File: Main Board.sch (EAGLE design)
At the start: 25 parts, among them IC1 TB6612FNG, U1 TPS61030RSAR

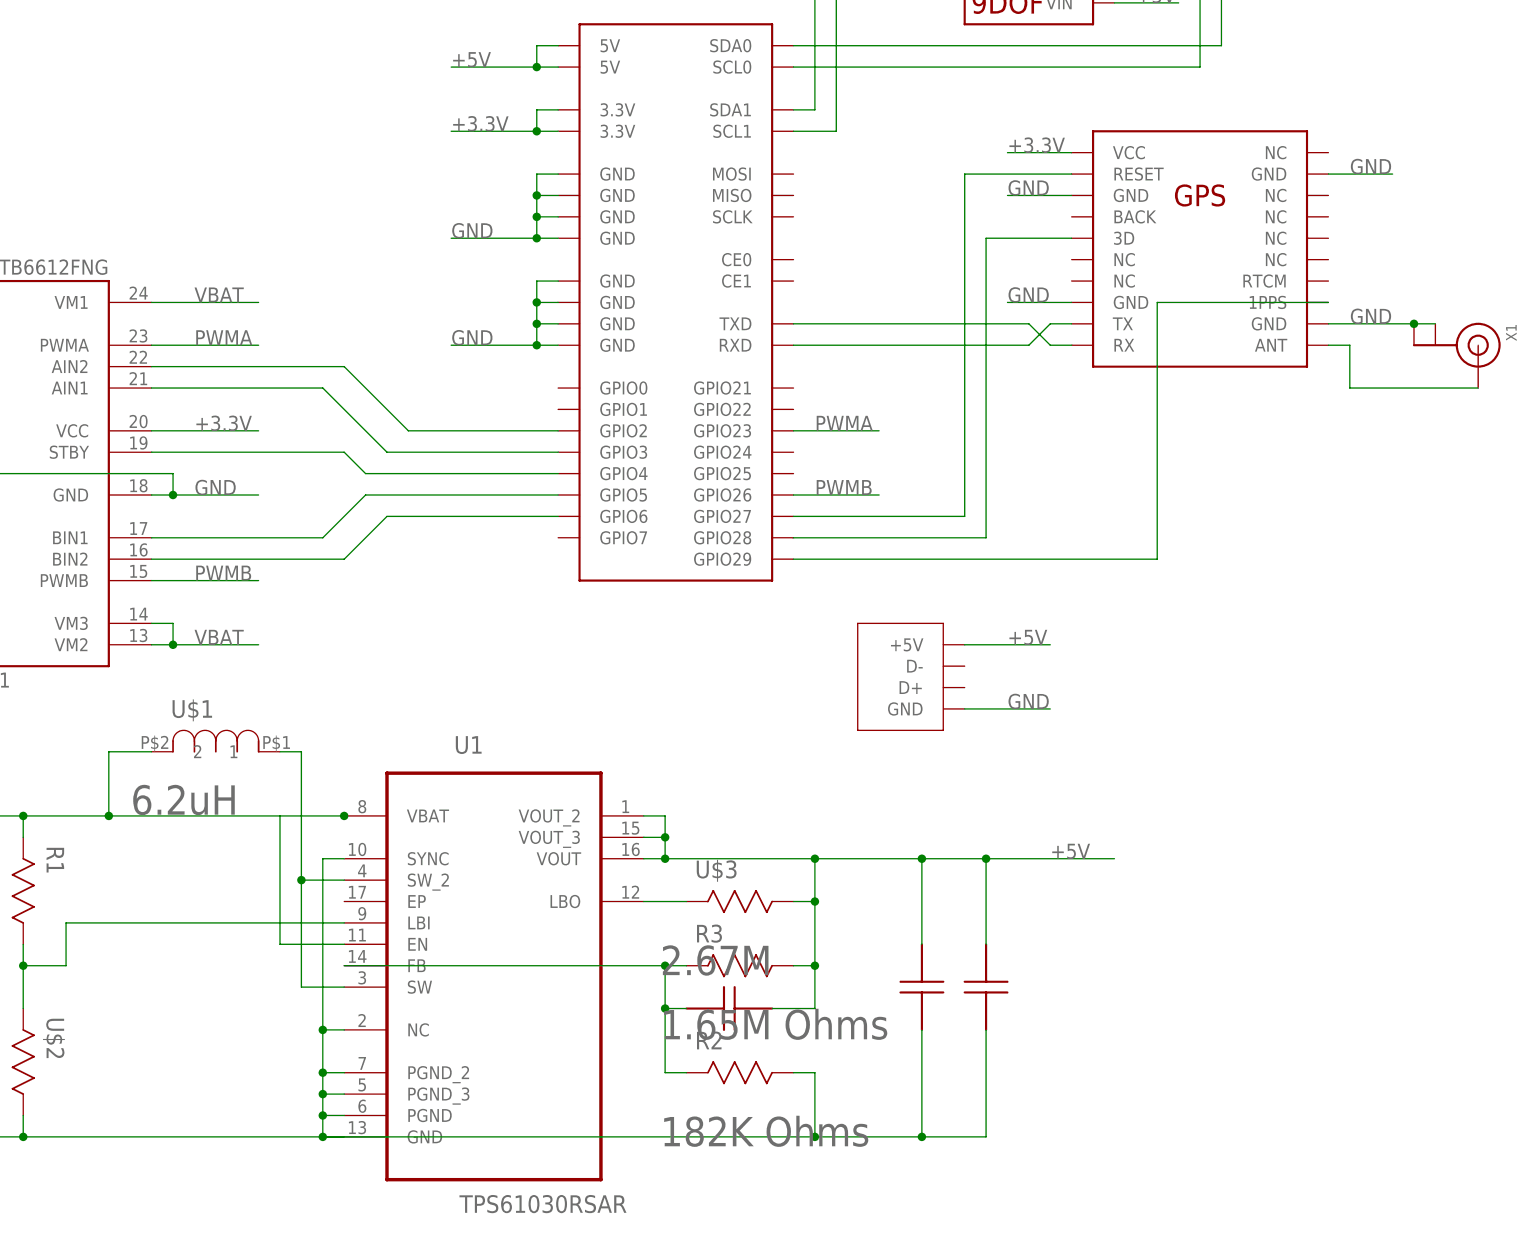
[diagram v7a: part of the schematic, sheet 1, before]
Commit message: Added Ground Pours
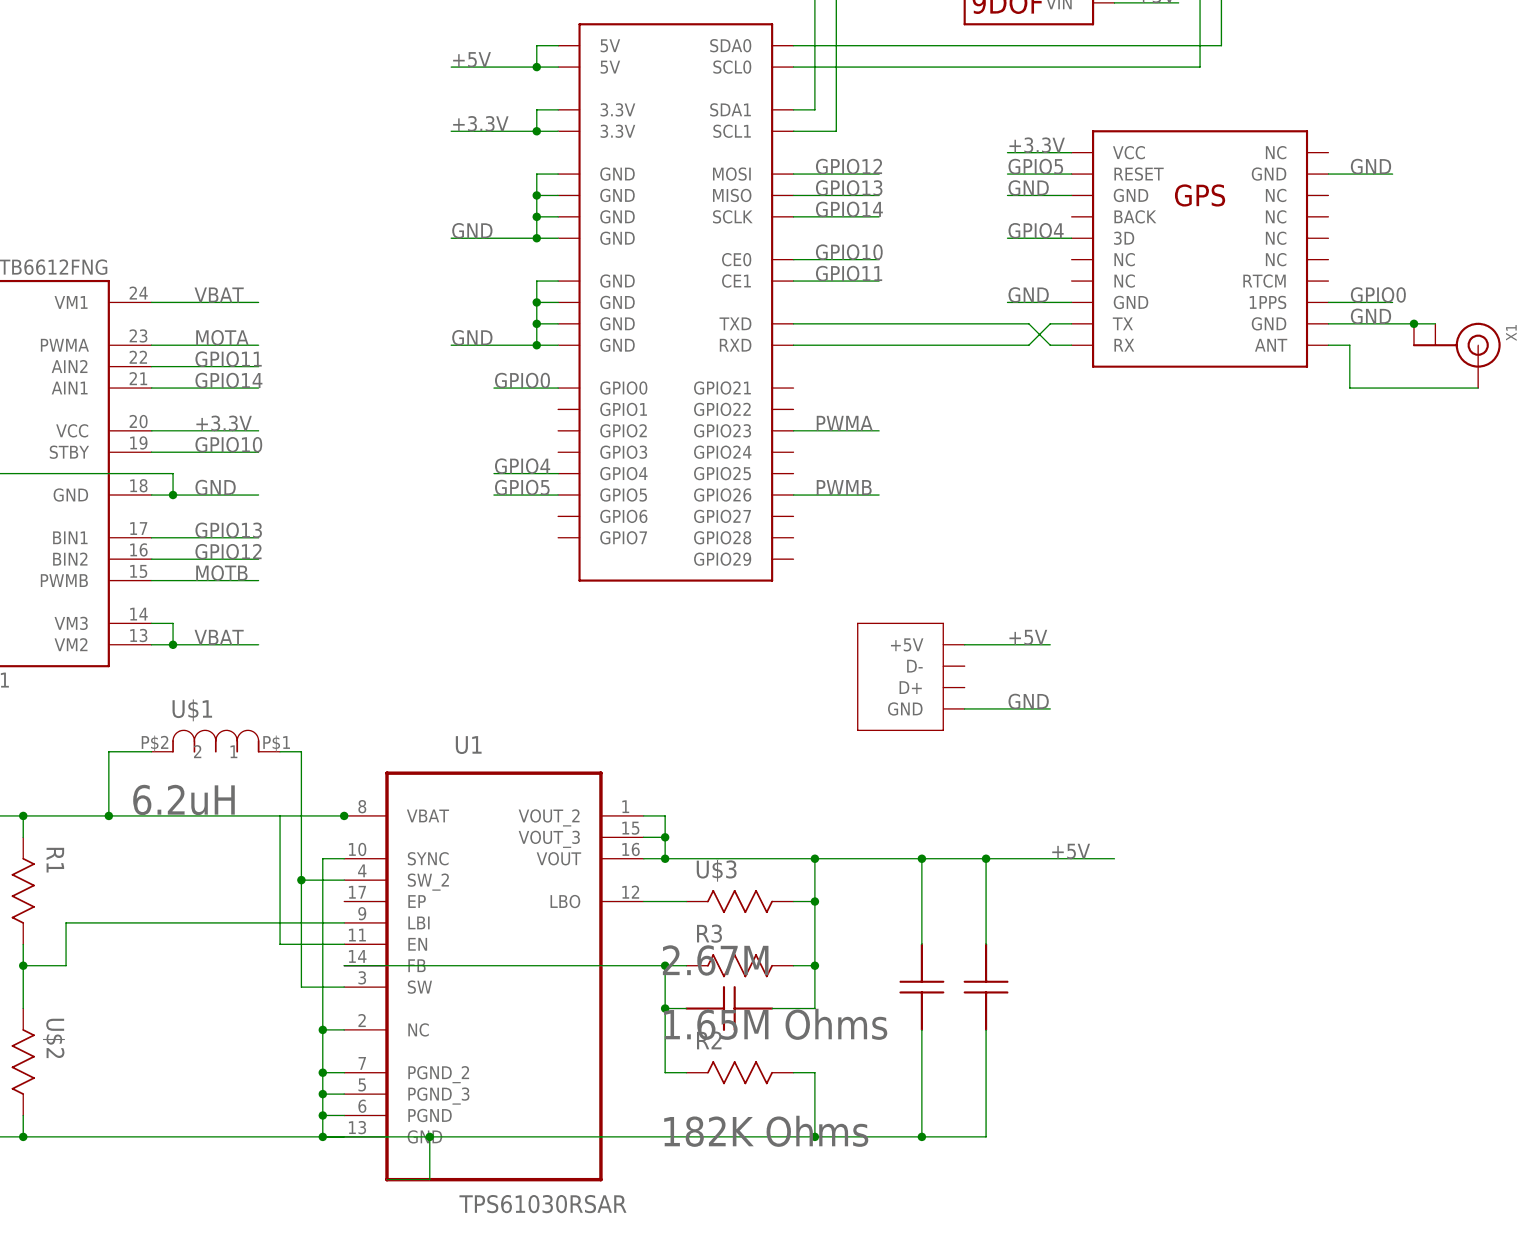
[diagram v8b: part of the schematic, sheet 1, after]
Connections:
- removed net N$15: IC1.AIN2, U$11.GPIO2
- removed net N$20: IC1.AIN1, U$11.GPIO3
- removed net N$21: IC1.STBY, U$11.GPIO4
- removed net N$22: IC1.BIN1, U$11.GPIO5
- removed net N$23: IC1.BIN2, U$11.GPIO6
- removed net N$5: U$11.GPIO27, U$5.RESET
- removed net N$6: U$11.GPIO28, U$5.3D
- removed net N$9: U$11.GPIO29, U$5.1PPS
- new net GPIO0: U$11.GPIO0, U$5.1PPS
- new net GPIO10: IC1.STBY, U$11.CE0
- new net GPIO11: IC1.AIN2, U$11.CE1
- new net GPIO12: IC1.BIN2, U$11.MOSI
- new net GPIO13: IC1.BIN1, U$11.MISO
- new net GPIO14: IC1.AIN1, U$11.SCLK
- new net GPIO4: U$11.GPIO4, U$5.3D
- new net GPIO5: U$11.GPIO5, U$5.RESET
- new net MOTA: IC1.PWMA
- new net MOTB: IC1.PWMB
- net PWMA: no longer IC1.PWMA
- net PWMB: no longer IC1.PWMB
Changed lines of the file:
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@@
 <wire x1="60.96" y1="-22.86" x2="53.34" y2="-22.86" width="0.1524" layer="91"/>
 <wire x1="53.34" y1="-22.86" x2="33.02" y2="-22.86" width="0.1524" layer="91"/>
-<wire x1="111.76" y1="-22.86" x2="170.18" y2="-22.86" width="0.1524" layer="91"/>
+<wire x1="111.76" y1="-22.86" x2="124.46" y2="-22.86" width="0.1524" layer="91"/>
 <label x="43.18" y="-22.86" size="1.778" layer="95"/>
 <pinref part="U$7" gate="G$1" pin="P$2"/>
+<wire x1="124.46" y1="-22.86" x2="170.18" y2="-22.86" width="0.1524" layer="91"/>
 <wire x1="170.18" y1="-22.86" x2="182.88" y2="-22.86" width="0.1524" layer="91"/>
 <wire x1="182.88" y1="-22.86" x2="190.5" y2="-22.86" width="0.1524" layer="91"/>
@@
 <junction x="25.4" y="-7.62"/>
 <junction x="33.02" y="-7.62"/>
+<wire x1="119.38" y1="-27.94" x2="124.46" y2="-27.94" width="0.1524" layer="91"/>
+<wire x1="124.46" y1="-27.94" x2="124.46" y2="-22.86" width="0.1524" layer="91"/>
+<junction x="124.46" y="-22.86"/>
 </segment>
 <segment>
@@
 </segment>
 </net>
-<net name="N$5" class="0">
-<segment>
-<wire x1="187.96" y1="50.8" x2="187.96" y2="91.44" width="0.1524" layer="91"/>
-<pinref part="U$5" gate="G$1" pin="RESET"/>
-<wire x1="187.96" y1="91.44" x2="200.66" y2="91.44" width="0.1524" layer="91"/>
-<pinref part="U$11" gate="G$1" pin="GPIO27"/>
-<wire x1="187.96" y1="50.8" x2="167.64" y2="50.8" width="0.1524" layer="91"/>
-</segment>
-</net>
-<net name="N$6" class="0">
-<segment>
-<wire x1="190.5" y1="48.26" x2="190.5" y2="83.82" width="0.1524" layer="91"/>
+<net name="GPIO4" class="0">
+<segment>
 <pinref part="U$5" gate="G$1" pin="3D"/>
-<wire x1="190.5" y1="83.82" x2="200.66" y2="83.82" width="0.1524" layer="91"/>
-<pinref part="U$11" gate="G$1" pin="GPIO28"/>
-<wire x1="190.5" y1="48.26" x2="167.64" y2="48.26" width="0.1524" layer="91"/>
+<wire x1="193.04" y1="83.82" x2="200.66" y2="83.82" width="0.1524" layer="91"/>
+<label x="193.04" y="83.82" size="1.778" layer="95"/>
+</segment>
+<segment>
+<pinref part="U$11" gate="G$1" pin="GPIO4"/>
+<wire x1="139.7" y1="55.88" x2="132.08" y2="55.88" width="0.1524" layer="91"/>
+<label x="132.08" y="55.88" size="1.778" layer="95"/>
 </segment>
 </net>
@@
 <pinref part="X1" gate="G$1" pin="SIGNAL"/>
 <wire x1="233.68" y1="66.04" x2="248.92" y2="66.04" width="0.1524" layer="91"/>
-</segment>
-</net>
-<net name="N$9" class="0">
-<segment>
-<pinref part="U$5" gate="G$1" pin="1PPS"/>
-<wire x1="231.14" y1="76.2" x2="210.82" y2="76.2" width="0.1524" layer="91"/>
-<wire x1="210.82" y1="76.2" x2="210.82" y2="45.72" width="0.1524" layer="91"/>
-<pinref part="U$11" gate="G$1" pin="GPIO29"/>
-<wire x1="210.82" y1="45.72" x2="167.64" y2="45.72" width="0.1524" layer="91"/>
 </segment>
 </net>
@@
 <label x="170.18" y="60.96" size="1.778" layer="95"/>
 </segment>
+</net>
+<net name="PWMB" class="0">
+<segment>
+<pinref part="U$11" gate="G$1" pin="GPIO26"/>
+<wire x1="167.64" y1="53.34" x2="177.8" y2="53.34" width="0.1524" layer="91"/>
+<label x="170.18" y="53.34" size="1.778" layer="95"/>
+</segment>
+</net>
+<net name="GPIO11" class="0">
+<segment>
+<pinref part="IC1" gate="G$1" pin="AIN2"/>
+<wire x1="104.14" y1="68.58" x2="91.44" y2="68.58" width="0.1524" layer="91"/>
+<label x="96.52" y="68.58" size="1.778" layer="95"/>
+</segment>
+<segment>
+<pinref part="U$11" gate="G$1" pin="CE1"/>
+<wire x1="167.64" y1="78.74" x2="177.8" y2="78.74" width="0.1524" layer="91"/>
+<label x="170.18" y="78.74" size="1.778" layer="95"/>
+</segment>
+</net>
+<net name="GPIO14" class="0">
+<segment>
+<pinref part="U$11" gate="G$1" pin="SCLK"/>
+<wire x1="167.64" y1="86.36" x2="177.8" y2="86.36" width="0.1524" layer="91"/>
+<label x="170.18" y="86.36" size="1.778" layer="95"/>
+</segment>
+<segment>
+<pinref part="IC1" gate="G$1" pin="AIN1"/>
+<wire x1="91.44" y1="66.04" x2="104.14" y2="66.04" width="0.1524" layer="91"/>
+<label x="96.52" y="66.04" size="1.778" layer="95"/>
+</segment>
+</net>
+<net name="GPIO13" class="0">
+<segment>
+<pinref part="IC1" gate="G$1" pin="BIN1"/>
+<wire x1="104.14" y1="48.26" x2="91.44" y2="48.26" width="0.1524" layer="91"/>
+<label x="96.52" y="48.26" size="1.778" layer="95"/>
+</segment>
+<segment>
+<pinref part="U$11" gate="G$1" pin="MISO"/>
+<wire x1="167.64" y1="88.9" x2="177.8" y2="88.9" width="0.1524" layer="91"/>
+<label x="170.18" y="88.9" size="1.778" layer="95"/>
+</segment>
+</net>
+<net name="GPIO12" class="0">
+<segment>
+<pinref part="IC1" gate="G$1" pin="BIN2"/>
+<wire x1="104.14" y1="45.72" x2="91.44" y2="45.72" width="0.1524" layer="91"/>
+<label x="96.52" y="45.72" size="1.778" layer="95"/>
+</segment>
+<segment>
+<pinref part="U$11" gate="G$1" pin="MOSI"/>
+<wire x1="177.8" y1="91.44" x2="167.64" y2="91.44" width="0.1524" layer="91"/>
+<label x="170.18" y="91.44" size="1.778" layer="95"/>
+</segment>
+</net>
+<net name="GPIO10" class="0">
+<segment>
+<pinref part="U$11" gate="G$1" pin="CE0"/>
+<wire x1="167.64" y1="81.28" x2="177.8" y2="81.28" width="0.1524" layer="91"/>
+<label x="170.18" y="81.28" size="1.778" layer="95"/>
+</segment>
+<segment>
+<pinref part="IC1" gate="G$1" pin="STBY"/>
+<wire x1="104.14" y1="58.42" x2="91.44" y2="58.42" width="0.1524" layer="91"/>
+<label x="96.52" y="58.42" size="1.778" layer="95"/>
+</segment>
+</net>
+<net name="MOTA" class="0">
 <segment>
 <pinref part="IC1" gate="G$1" pin="PWMA"/>
@@
 </segment>
 </net>
-<net name="PWMB" class="0">
-<segment>
-<pinref part="U$11" gate="G$1" pin="GPIO26"/>
-<wire x1="167.64" y1="53.34" x2="177.8" y2="53.34" width="0.1524" layer="91"/>
-<label x="170.18" y="53.34" size="1.778" layer="95"/>
-</segment>
+<net name="MOTB" class="0">
 <segment>
 <pinref part="IC1" gate="G$1" pin="PWMB"/>
@@
 </segment>
 </net>
-<net name="N$15" class="0">
-<segment>
-<pinref part="U$11" gate="G$1" pin="GPIO2"/>
-<wire x1="139.7" y1="60.96" x2="121.92" y2="60.96" width="0.1524" layer="91"/>
-<wire x1="121.92" y1="60.96" x2="114.3" y2="68.58" width="0.1524" layer="91"/>
-<pinref part="IC1" gate="G$1" pin="AIN2"/>
-<wire x1="114.3" y1="68.58" x2="91.44" y2="68.58" width="0.1524" layer="91"/>
-</segment>
-</net>
-<net name="N$20" class="0">
-<segment>
-<pinref part="IC1" gate="G$1" pin="AIN1"/>
-<wire x1="91.44" y1="66.04" x2="111.76" y2="66.04" width="0.1524" layer="91"/>
-<wire x1="111.76" y1="66.04" x2="119.38" y2="58.42" width="0.1524" layer="91"/>
-<pinref part="U$11" gate="G$1" pin="GPIO3"/>
-<wire x1="119.38" y1="58.42" x2="139.7" y2="58.42" width="0.1524" layer="91"/>
-</segment>
-</net>
-<net name="N$21" class="0">
-<segment>
-<pinref part="U$11" gate="G$1" pin="GPIO4"/>
-<wire x1="139.7" y1="55.88" x2="116.84" y2="55.88" width="0.1524" layer="91"/>
-<wire x1="116.84" y1="55.88" x2="114.3" y2="58.42" width="0.1524" layer="91"/>
-<pinref part="IC1" gate="G$1" pin="STBY"/>
-<wire x1="114.3" y1="58.42" x2="91.44" y2="58.42" width="0.1524" layer="91"/>
-</segment>
-</net>
-<net name="N$22" class="0">
+<net name="GPIO5" class="0">
+<segment>
+<pinref part="U$5" gate="G$1" pin="RESET"/>
+<wire x1="193.04" y1="91.44" x2="200.66" y2="91.44" width="0.1524" layer="91"/>
+<label x="193.04" y="91.44" size="1.778" layer="95"/>
+</segment>
 <segment>
 <pinref part="U$11" gate="G$1" pin="GPIO5"/>
-<wire x1="139.7" y1="53.34" x2="116.84" y2="53.34" width="0.1524" layer="91"/>
-<wire x1="116.84" y1="53.34" x2="111.76" y2="48.26" width="0.1524" layer="91"/>
-<pinref part="IC1" gate="G$1" pin="BIN1"/>
-<wire x1="111.76" y1="48.26" x2="91.44" y2="48.26" width="0.1524" layer="91"/>
-</segment>
-</net>
-<net name="N$23" class="0">
-<segment>
-<pinref part="U$11" gate="G$1" pin="GPIO6"/>
-<wire x1="139.7" y1="50.8" x2="119.38" y2="50.8" width="0.1524" layer="91"/>
-<wire x1="119.38" y1="50.8" x2="114.3" y2="45.72" width="0.1524" layer="91"/>
-<pinref part="IC1" gate="G$1" pin="BIN2"/>
-<wire x1="114.3" y1="45.72" x2="91.44" y2="45.72" width="0.1524" layer="91"/>
-</segment>
-</net>
+<wire x1="139.7" y1="53.34" x2="132.08" y2="53.34" width="0.1524" layer="91"/>
+<label x="132.08" y="53.34" size="1.778" layer="95"/>
+</segment>
+</net>
+<net name="GPIO0" class="0">
+<segment>
+<pinref part="U$5" gate="G$1" pin="1PPS"/>
+<wire x1="231.14" y1="76.2" x2="238.76" y2="76.2" width="0.1524" layer="91"/>
+<label x="233.68" y="76.2" size="1.778" layer="95"/>
+</segment>
+<segment>
+<pinref part="U$11" gate="G$1" pin="GPIO0"/>
+<wire x1="139.7" y1="66.04" x2="132.08" y2="66.04" width="0.1524" layer="91"/>
+<label x="132.08" y="66.04" size="1.778" layer="95"/>
+</segment>
+</net>
